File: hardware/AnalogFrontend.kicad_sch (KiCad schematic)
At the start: 26 parts, among them J1 Exp1, J2 Exp2, J3 Exp3, J4 Exp4, J5 Exp1_Spare, J6 Exp2_Spare, J7 Exp3_Spare, J8 Exp4_Spare, U14 AD7718, U4 AD7718, Y1 SC32A-12.5PF20PPM, Y2 SC32A-12.5PF20PPM

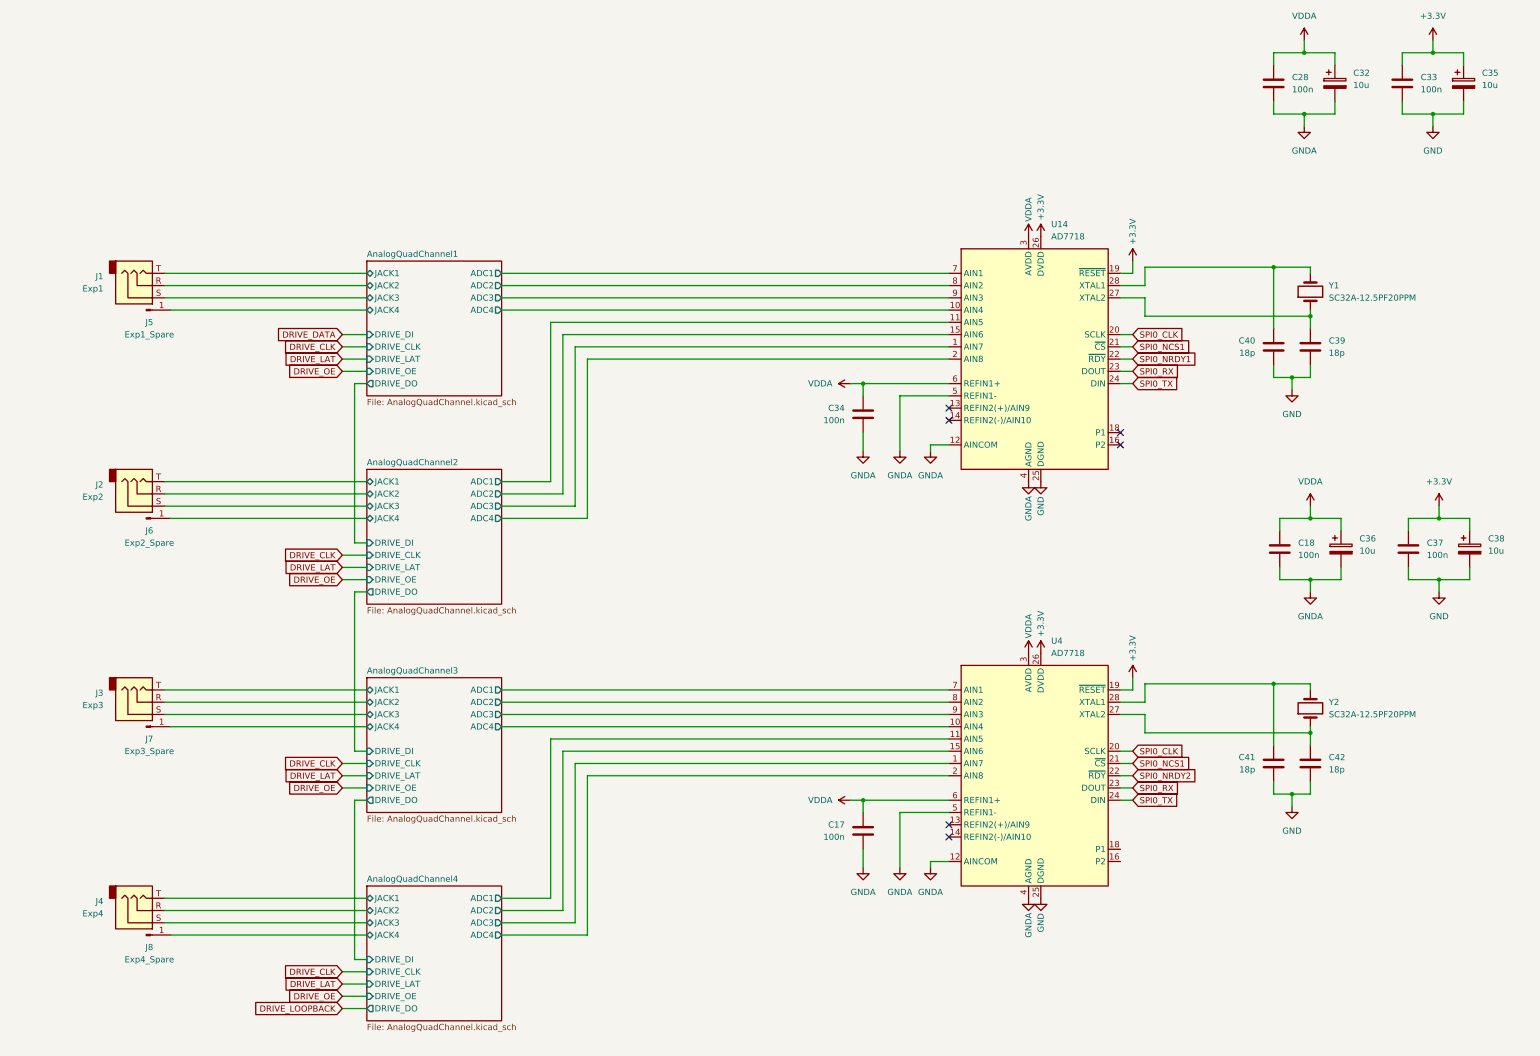
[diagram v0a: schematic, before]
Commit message: updated Power input on schematic
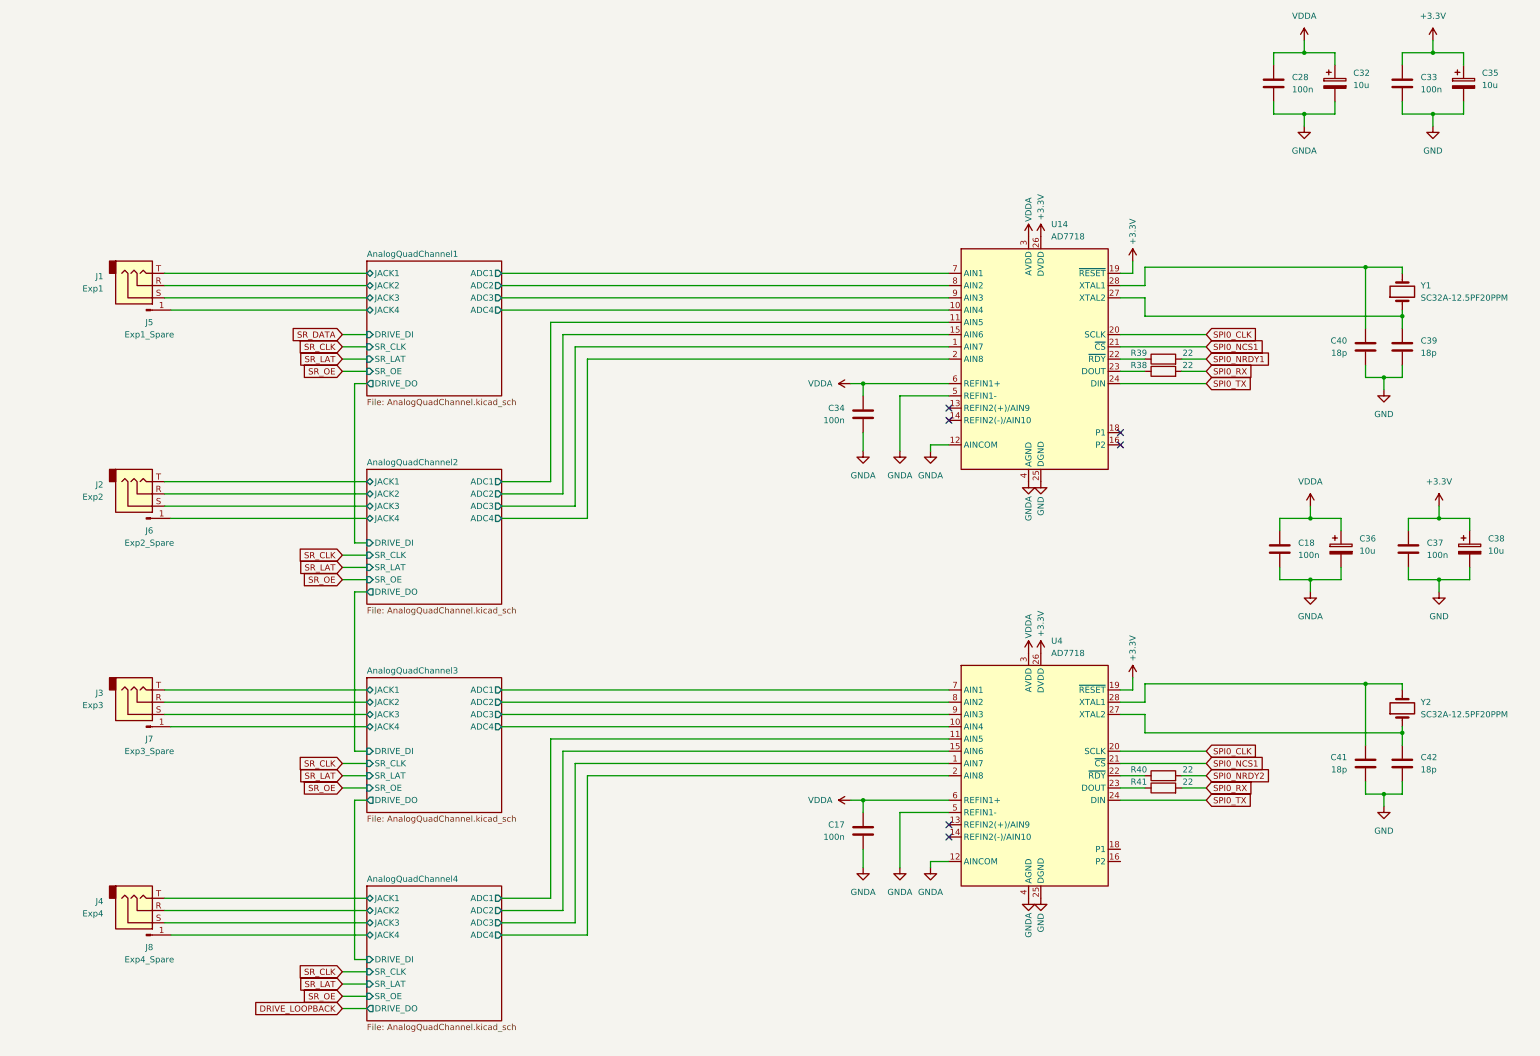
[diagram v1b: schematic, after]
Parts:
- added R38, R39, R40, R41: 22, symbol Device:R
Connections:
- net SPI0_NRDY1: now also R39.2; no longer U14.22 (~{RDY})
- net SPI0_NRDY2: now also R40.2; no longer U4.22 (~{RDY})
- net SPI0_RX: now also R38.2, R41.2; no longer U14.23 (DOUT), U4.23 (DOUT)
- new net: R39.1, U14.22 (~{RDY})
- new net: R38.1, U14.23 (DOUT)
- new net: R40.1, U4.22 (~{RDY})
- new net: R41.1, U4.23 (DOUT)
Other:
- sheet AnalogQuadChannel1 ports: added SR_CLK, SR_LAT, SR_OE; removed DRIVE_CLK, DRIVE_LAT, DRIVE_OE
- sheet AnalogQuadChannel2 ports: added SR_CLK, SR_LAT, SR_OE; removed DRIVE_CLK, DRIVE_LAT, DRIVE_OE
- sheet AnalogQuadChannel3 ports: added SR_CLK, SR_LAT, SR_OE; removed DRIVE_CLK, DRIVE_LAT, DRIVE_OE
- sheet AnalogQuadChannel4 ports: added SR_CLK, SR_LAT, SR_OE; removed DRIVE_CLK, DRIVE_LAT, DRIVE_OE
- moved on the sheet: C39, C40, C41, C42, Y1, Y2

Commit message: reworked power protection circuit and fixed ERC errors
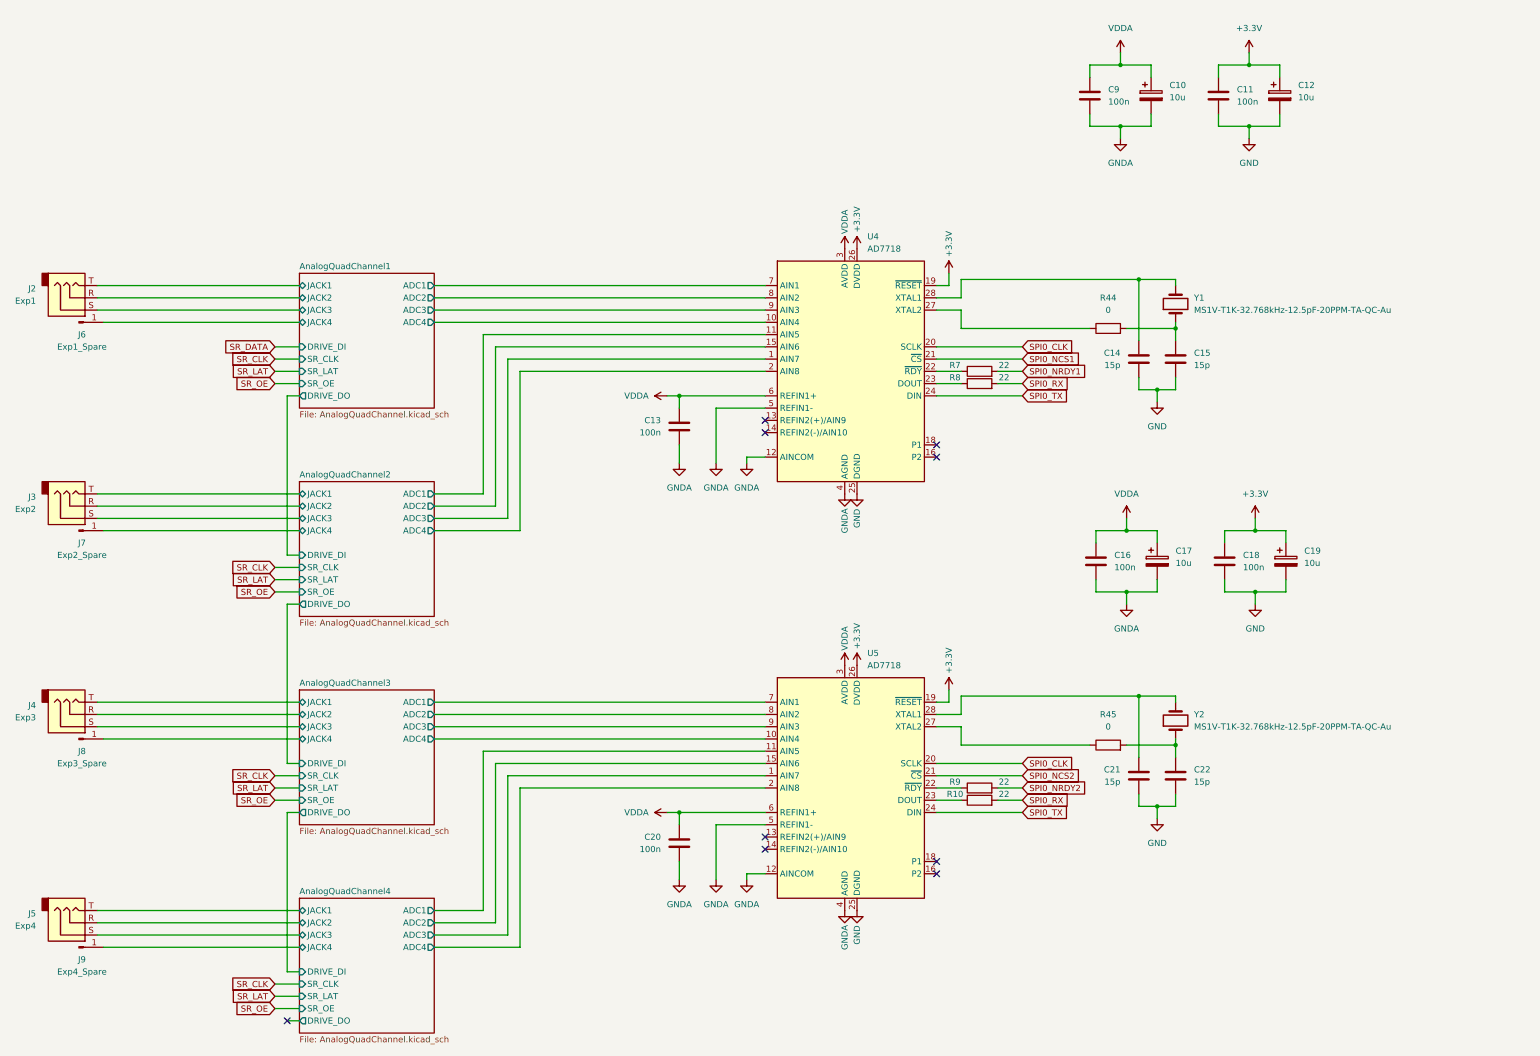
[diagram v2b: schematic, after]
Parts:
- added R44, R45: 0, Resistor_SMD:R_0603_1608Metric, symbol Device:R
- C10: renamed from C32; footprint Capacitor_SMD:C_0603_1608Metric -> Capacitor_SMD:C_1210_3225Metric
- C12: renamed from C35; footprint Capacitor_SMD:C_0603_1608Metric -> Capacitor_SMD:C_1210_3225Metric
- C14: renamed from C40; value 18p -> 15p
- C15: renamed from C39; value 18p -> 15p
- C17: renamed from C36; footprint Capacitor_SMD:C_0603_1608Metric -> Capacitor_SMD:C_1210_3225Metric
- C19: renamed from C38; footprint Capacitor_SMD:C_0603_1608Metric -> Capacitor_SMD:C_1210_3225Metric
- C21: renamed from C41; value 18p -> 15p
- C22: renamed from C42; value 18p -> 15p
- R10: renamed from R41; footprint (none) -> Resistor_SMD:R_0603_1608Metric
- R7: renamed from R39; footprint (none) -> Resistor_SMD:R_0603_1608Metric
- R8: renamed from R38; footprint (none) -> Resistor_SMD:R_0603_1608Metric
- R9: renamed from R40; footprint (none) -> Resistor_SMD:R_0603_1608Metric
- Y1, Y2: value SC32A-12.5PF20PPM -> MS1V-T1K-32.768kHz-12.5pF-20PPM-TA-QC-Au; footprint (none) -> Crystal:Crystal_SMD_3215-2Pin_3.2x1.5mm
- renumbered C33 to C11, C34 to C13, C18 to C16, C37 to C18, C17 to C20, C28 to C9, J1 to J2, J2 to J3, J3 to J4, J4 to J5, J5 to J6, J6 to J7, J7 to J8, J8 to J9, U14 to U4, U4 to U5
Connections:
- net SPI0_NCS1: no longer U5.21 (~{CS})
- net at C15.1, Y1.1: now also R44.2; no longer U4.27 (XTAL2)
- net at C22.1, Y2.1: now also R45.2; no longer U5.27 (XTAL2)
- new net: R44.1, U4.27 (XTAL2)
- new net: R45.1, U5.27 (XTAL2)
- new net SPI0_NCS2: U5.21 (~{CS})
- no-connect marks 6 -> 9
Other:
- moved on the sheet: C10, C11, C12, C13, C14, C15, C16, C17, C18, C19, C20, C21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

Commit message: added basic PCB ordering
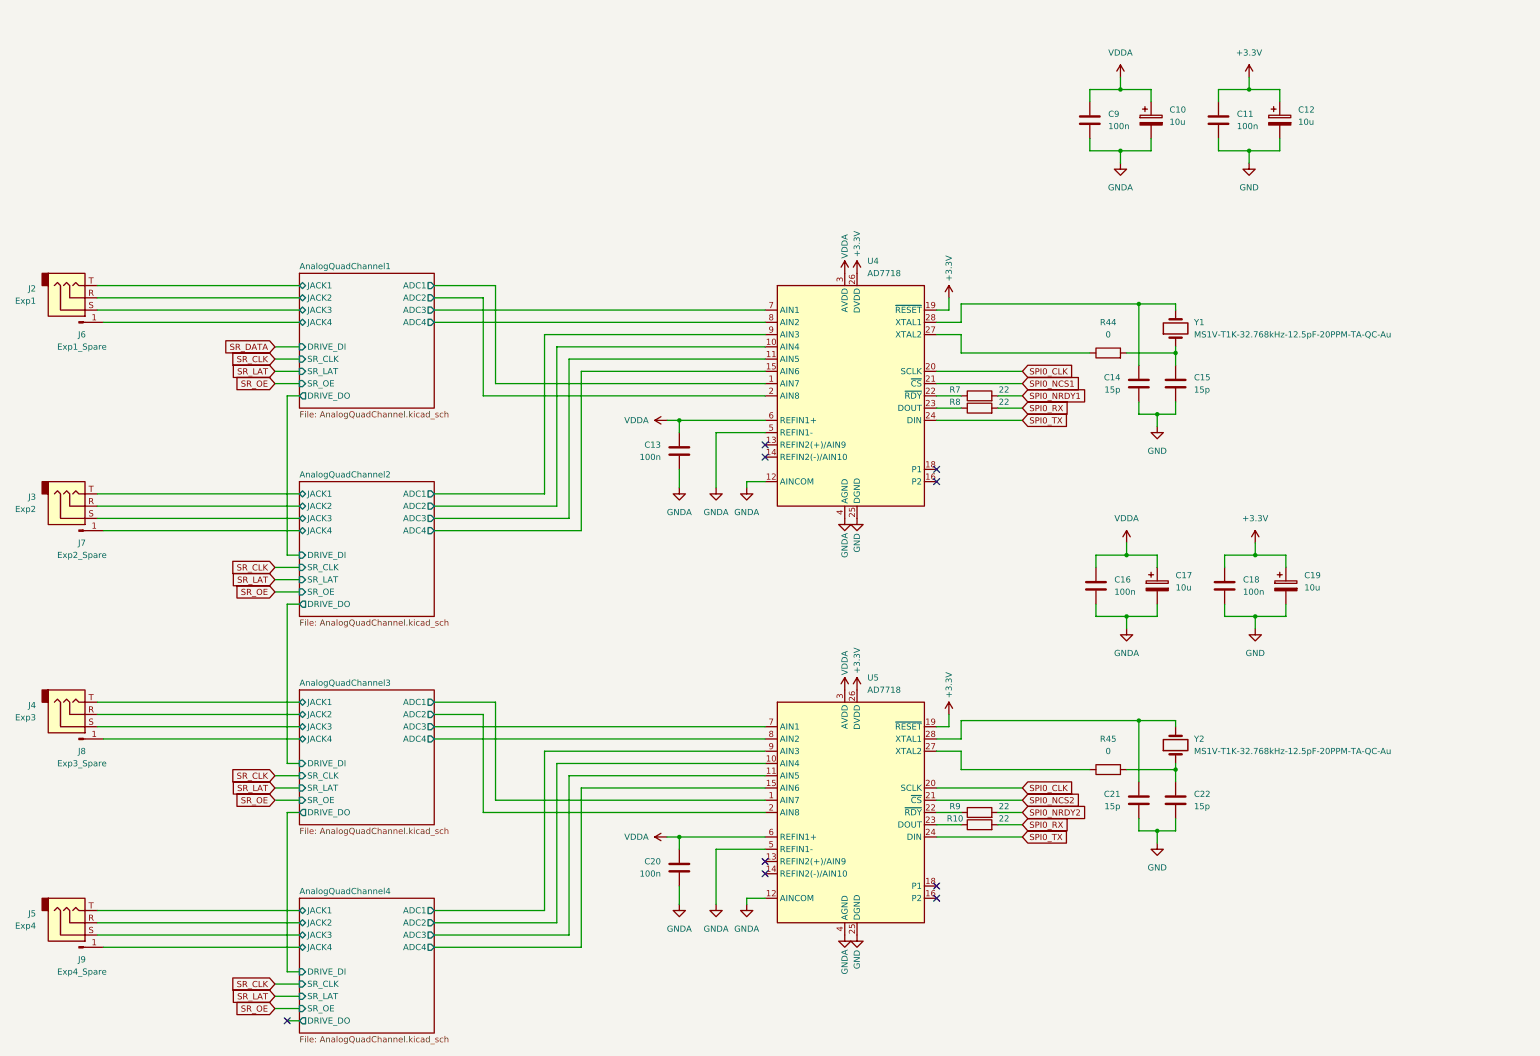
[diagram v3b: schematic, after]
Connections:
- net AnalogQuadChannel1/ADC1: now also U4.1 (AIN7); no longer U4.7 (AIN1)
- net AnalogQuadChannel1/ADC2: now also U4.2 (AIN8); no longer U4.8 (AIN2)
- net AnalogQuadChannel1/ADC3: now also U4.7 (AIN1); no longer U4.9 (AIN3)
- net AnalogQuadChannel1/ADC4: now also U4.8 (AIN2); no longer U4.10 (AIN4)
- net AnalogQuadChannel2/ADC1: now also U4.9 (AIN3); no longer U4.11 (AIN5)
- net AnalogQuadChannel2/ADC2: now also U4.10 (AIN4); no longer U4.15 (AIN6)
- net AnalogQuadChannel2/ADC3: now also U4.11 (AIN5); no longer U4.1 (AIN7)
- net AnalogQuadChannel2/ADC4: now also U4.15 (AIN6); no longer U4.2 (AIN8)
- net AnalogQuadChannel3/ADC1: now also U5.1 (AIN7); no longer U5.7 (AIN1)
- net AnalogQuadChannel3/ADC2: now also U5.2 (AIN8); no longer U5.8 (AIN2)
- net AnalogQuadChannel3/ADC3: now also U5.7 (AIN1); no longer U5.9 (AIN3)
- net AnalogQuadChannel3/ADC4: now also U5.8 (AIN2); no longer U5.10 (AIN4)
- net AnalogQuadChannel4/ADC1: now also U5.9 (AIN3); no longer U5.11 (AIN5)
- net AnalogQuadChannel4/ADC2: now also U5.10 (AIN4); no longer U5.15 (AIN6)
- net AnalogQuadChannel4/ADC3: now also U5.11 (AIN5); no longer U5.1 (AIN7)
- net AnalogQuadChannel4/ADC4: now also U5.15 (AIN6); no longer U5.2 (AIN8)
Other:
- moved on the sheet: C10, C11, C12, C13, C14, C15, C16, C17, C18, C19, C20, C21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

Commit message: added all footprints, updated to 0805, added layout for Jacks
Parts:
- removed C12, C19: 10u, Capacitor_SMD:C_1210_3225Metric, symbol Device:C_Polarized
- removed J6: Exp1_Spare, symbol Connector:Conn_01x01_Pin
- removed J7: Exp2_Spare, symbol Connector:Conn_01x01_Pin
- removed J8: Exp3_Spare, symbol Connector:Conn_01x01_Pin
- removed J9: Exp4_Spare, symbol Connector:Conn_01x01_Pin
- C11, C13, C14, C15, C16, C18, C20, C21, C22, C9: footprint Capacitor_SMD:C_0603_1608Metric -> Capacitor_SMD:C_0805_2012Metric
- J2, J3, J4, J5: footprint (none) -> Jack_6.35mm_Neutrik_NMJ6HFD4_Horizontal:Jack_6.35mm_Neutrik_NMJ6HFD4_Horizontal; symbol Connector_Audio:AudioJack3 -> Connector_Audio:AudioJack3_Switch
- R10, R44, R45, R7, R8, R9: footprint Resistor_SMD:R_0603_1608Metric -> Resistor_SMD:R_0805_2012Metric
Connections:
- net AnalogQuadChannel1/JACK4: now also J2.TN
- net AnalogQuadChannel2/JACK4: now also J3.TN
- net AnalogQuadChannel3/JACK4: now also J4.TN
- net AnalogQuadChannel4/JACK4: now also J5.TN
- no-connect marks 9 -> 17
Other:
- sheet AnalogQuadChannel1 ports: added SR_DATA; removed DRIVE_DI
- sheet AnalogQuadChannel2 ports: added SR_DATA; removed DRIVE_DI
- sheet AnalogQuadChannel3 ports: added SR_DATA; removed DRIVE_DI
- sheet AnalogQuadChannel4 ports: added SR_DATA; removed DRIVE_DI
- moved on the sheet: C11, C18
